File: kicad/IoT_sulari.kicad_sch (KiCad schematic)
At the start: 21 parts, among them J1 73412-0110, J2 73412-0110, SW1 SW_SPST, U2 NRF9160-SICA-B1A-R

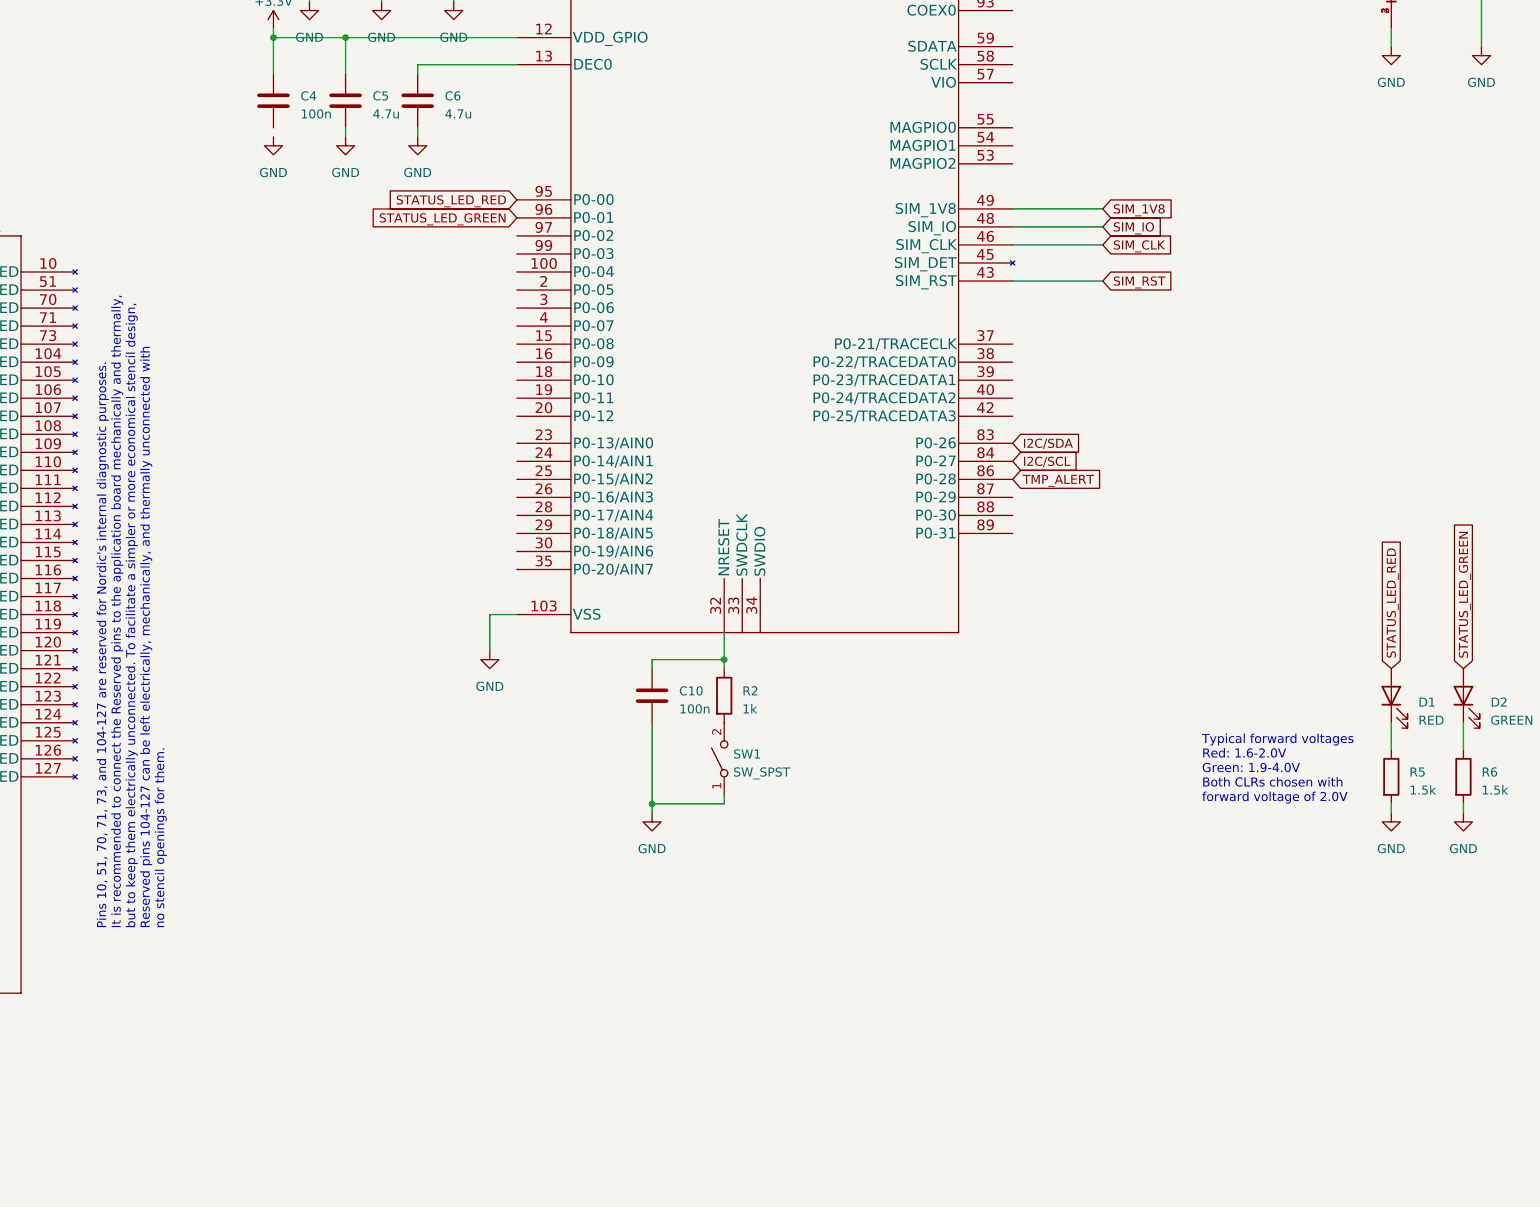
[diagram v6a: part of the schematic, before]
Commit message: Added buttons and connectors
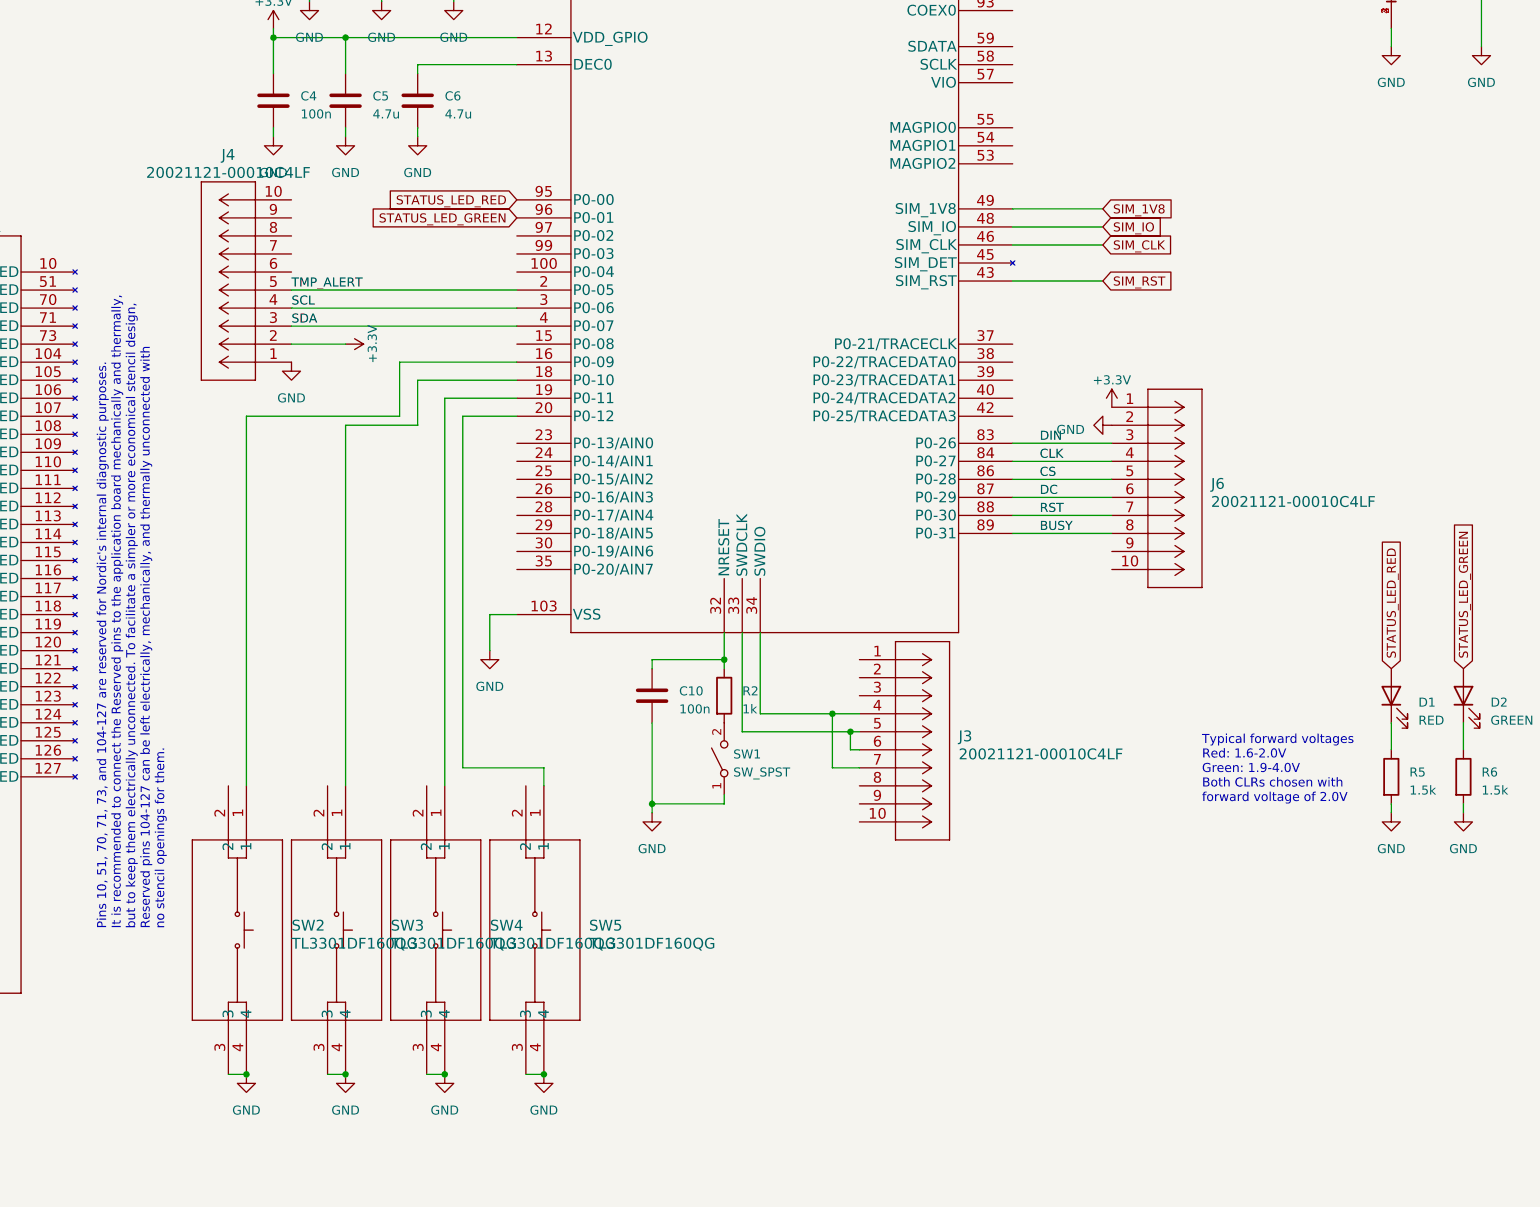
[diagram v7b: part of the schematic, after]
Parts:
- added J3, J4, J6: 20021121-00010C4LF, CONN_00010C4LF_AMP, symbol 20021121-00010C4LF:20021121-00010C4LF
- added SW2, SW3, SW4, SW5: TL3301DF160QG, SOIC4_TL3301DF160QG_EWI, symbol TL3301DF160QG:TL3301DF160QG
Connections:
- net +3.3V: now also J4.2, J6.1
- net GND: now also C4.2, J4.1, J6.2, SW2.3, SW2.4, SW3.3, SW3.4, SW4.3, SW4.4, SW5.3, SW5.4
- net TMP_ALERT: now also U2.2 (P0-05), J4.5; no longer U2.86 (P0-28)
- net at U2.16 (P0-09): now also SW2.1
- net at U2.18 (P0-10): now also SW3.1
- net at U2.19 (P0-11): now also SW4.1
- net at U2.20 (P0-12): now also SW5.1
- net SCL: now reaches U2.3 (P0-06)
- net SCL: now also J4.4
- net at U2.33 (SWDCLK): now also J3.5, J3.6
- net at U2.34 (SWDIO): now also J3.4, J3.7
- net SDA: now reaches U2.4 (P0-07)
- net SDA: now also J4.3
- net DC: now reaches U2.87 (P0-29)
- net DC: now also J6.6
- net RST: now reaches U2.88 (P0-30)
- net RST: now also J6.7
- net BUSY: now reaches U2.89 (P0-31)
- net BUSY: now also J6.8
- net I2C/SCL renamed CLK
- net CLK: now also J6.4
- net I2C/SDA renamed DIN
- net DIN: now also J6.3
- new net CS: J6.5, U2.86 (P0-28)

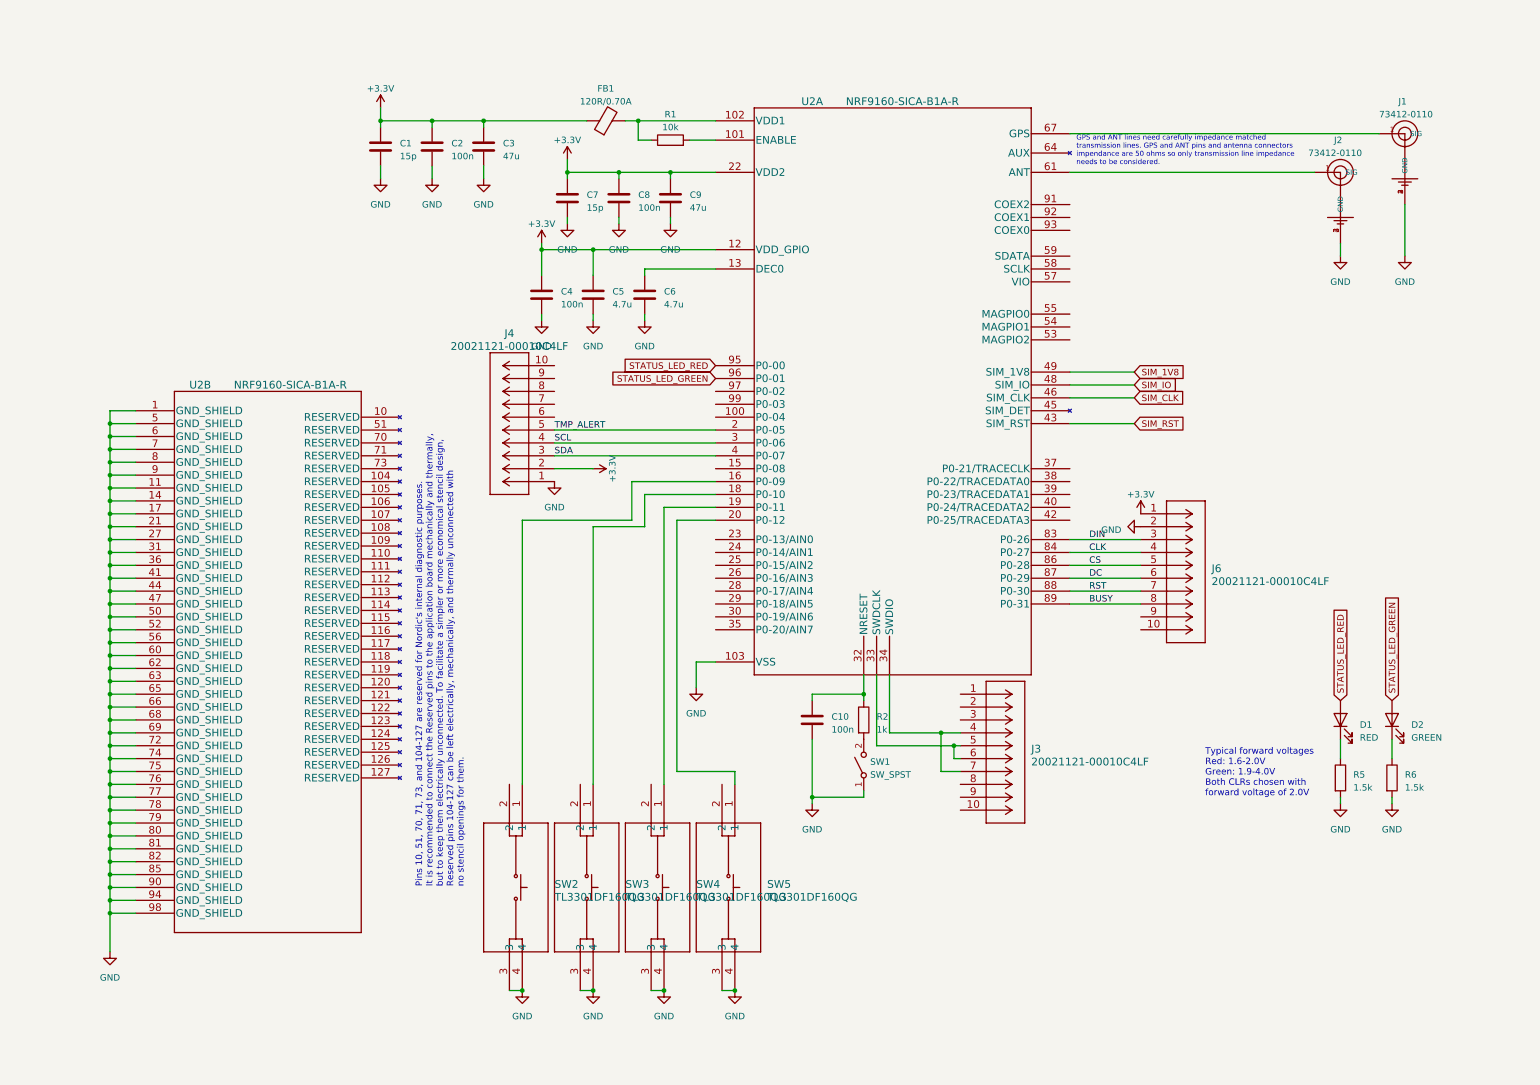
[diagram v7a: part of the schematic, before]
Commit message: schematic editing, led selection
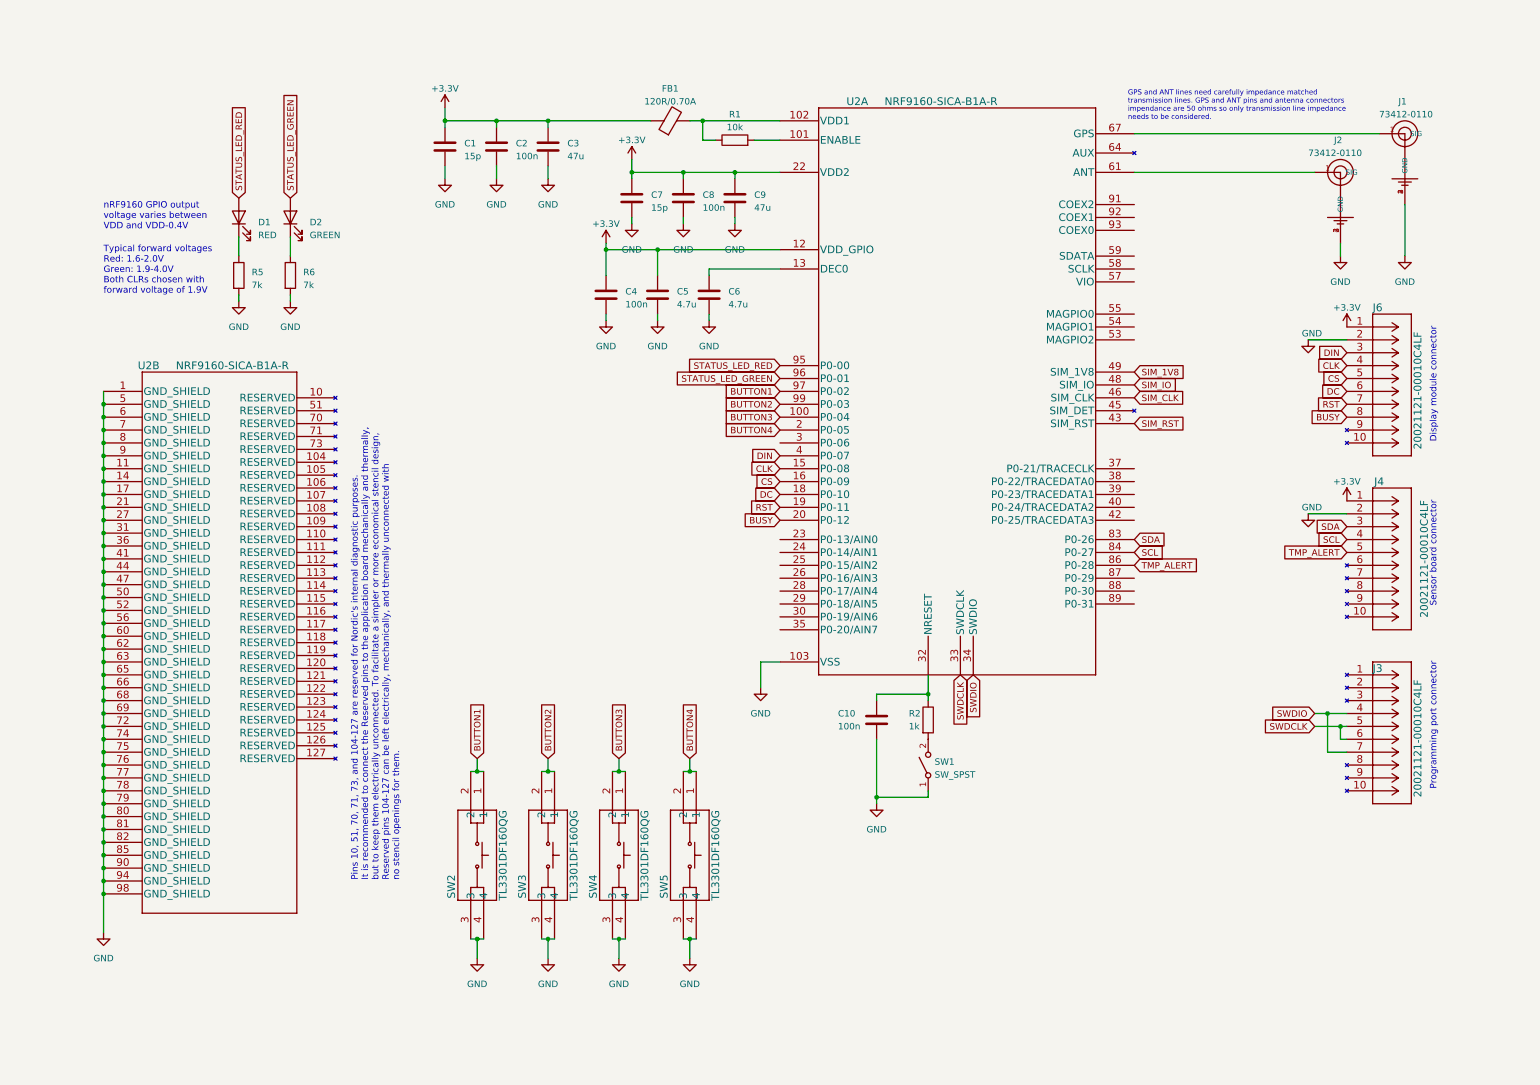
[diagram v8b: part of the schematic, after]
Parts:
- D1: footprint (none) -> LED_SMD:LED_0603_1608Metric_Pad1.05x0.95mm_HandSolder; Digikey (none) -> 1080-1400-1-ND
- D2: footprint (none) -> LED_SMD:LED_0603_1608Metric_Pad1.05x0.95mm_HandSolder; Digikey (none) -> 492-2523-1-ND
- R5, R6: value 1.5k -> 7k
- SW2, SW3, SW4, SW5: footprint SOIC4_TL3301DF160QG_EWI -> TL3301DF160QG:TL3301DF160QG
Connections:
- net +3.3V: now also J4.1; no longer J4.2
- net BUSY: now also U2.20 (P0-12); no longer U2.89 (P0-31)
- net CLK: now also U2.15 (P0-08); no longer U2.84 (P0-27)
- net CS: now also U2.16 (P0-09); no longer U2.86 (P0-28)
- net DC: now also U2.18 (P0-10); no longer U2.87 (P0-29)
- net DIN: now also U2.4 (P0-07); no longer U2.83 (P0-26)
- net GND: now also J4.2; no longer J4.1
- net RST: now also U2.19 (P0-11); no longer U2.88 (P0-30)
- net SCL: now also U2.84 (P0-27); no longer U2.3 (P0-06)
- net SDA: now also U2.83 (P0-26); no longer U2.4 (P0-07)
- net TMP_ALERT: now also U2.86 (P0-28); no longer U2.2 (P0-05)
- net BUTTON3: now reaches SW4.1
- net BUTTON3: now also SW4.2, U2.100 (P0-04); no longer U2.19 (P0-11)
- net BUTTON1: now reaches SW2.1
- net BUTTON1: now also SW2.2, U2.97 (P0-02); no longer U2.16 (P0-09)
- net BUTTON2: now reaches SW3.1
- net BUTTON2: now also SW3.2, U2.99 (P0-03); no longer U2.18 (P0-10)
- net BUTTON4: now reaches SW5.1
- net BUTTON4: now also SW5.2, U2.2 (P0-05); no longer U2.20 (P0-12)
- net SWDCLK: now reaches J3.5, J3.6, U2.33 (SWDCLK)
- net SWDIO: now reaches J3.4, J3.7, U2.34 (SWDIO)
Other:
- note added: "Display module connector"
- note added: "Programming port connector"
- note added: "Sensor board connector"
- note added: "Typical forward voltages Red: 1.6-2.0V Green: 1.9-4.0V Both CLRs chosen with forward voltage of 1.9V"
- note added: "nRF9160 GPIO output voltage varies between VDD and VDD-0.4V"
- note removed: "Typical forward voltages Red: 1.6-2.0V Green: 1.9-4.0V Both CLRs chosen with forward voltage of 2.0V"
- moved on the sheet: C1, C10, C2, C3, C4, C5, C6, C7, C8, C9, D1, D2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
